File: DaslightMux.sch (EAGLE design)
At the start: 8 parts, among them U1 XC9572XL_TQ100

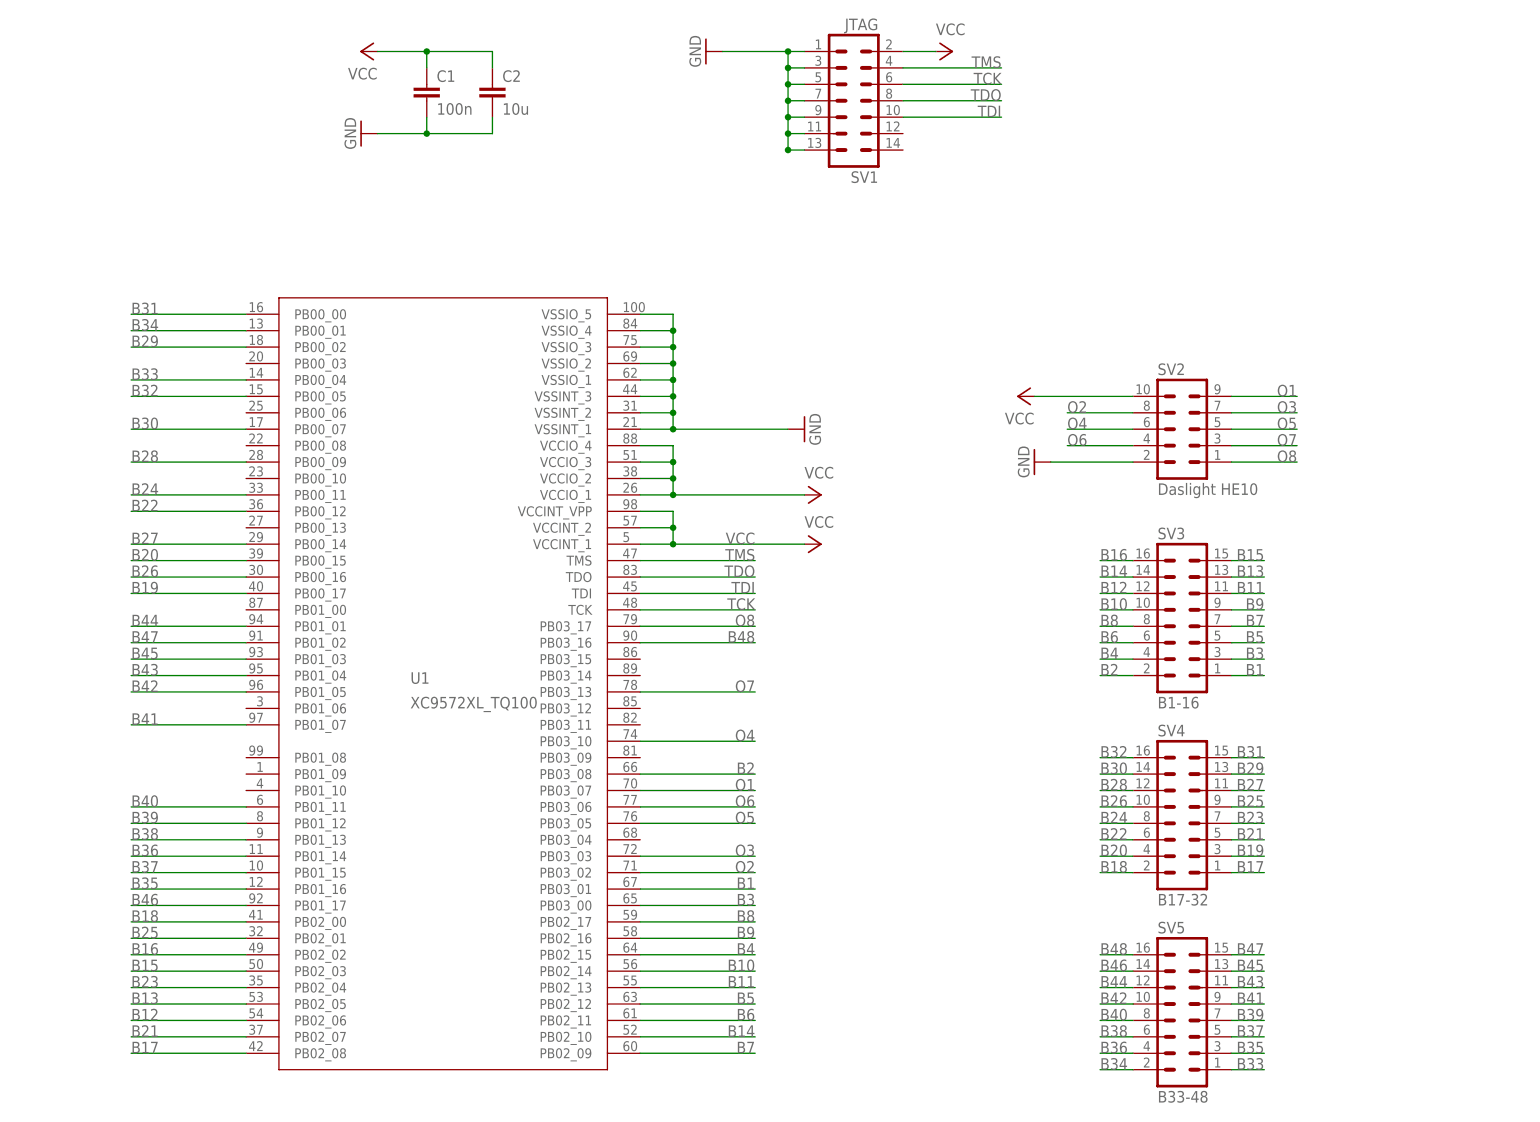
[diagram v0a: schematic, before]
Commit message: Cleanup, enclosure.
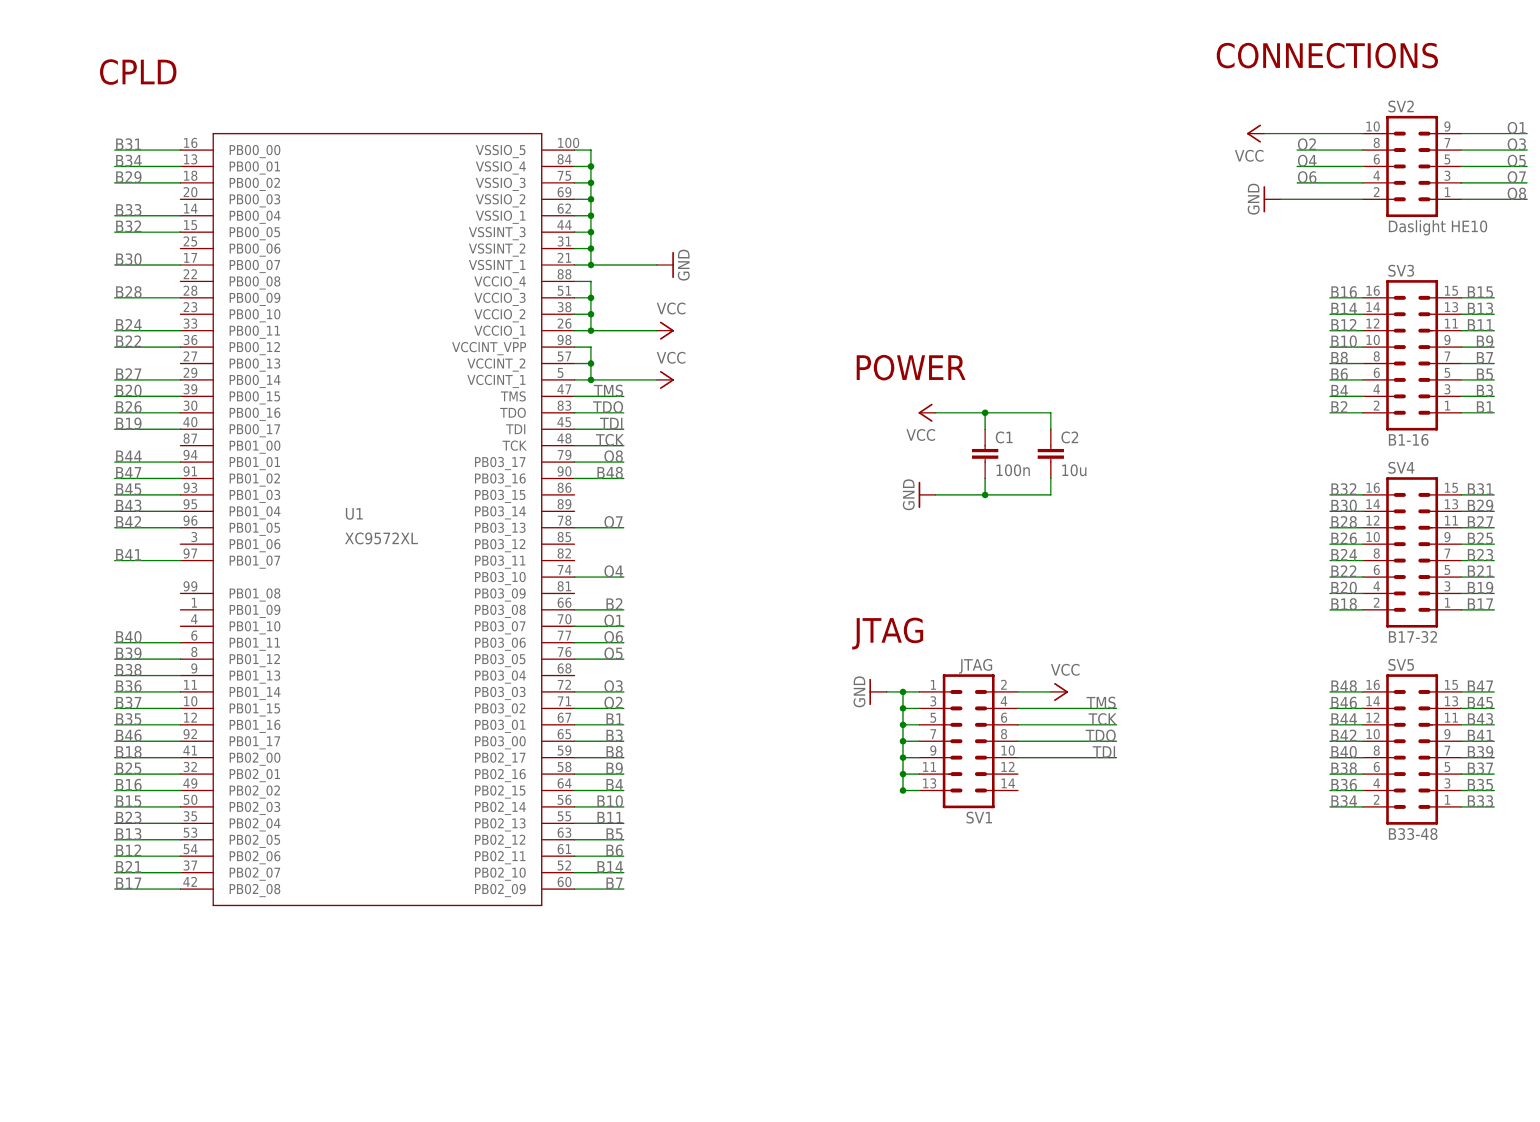
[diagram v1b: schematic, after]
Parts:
- U1: value XC9572XL_TQ100 -> XC9572XL
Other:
- note added: "CONNECTIONS"
- note added: "CPLD"
- note added: "JTAG"
- note added: "POWER"
- moved on the sheet: C1, C2, SV1, SV2, SV3, SV4, SV5, U1

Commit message: Schematic & enclosure
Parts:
- added EXT_VCC, GND: LSP10, solpad:LSP10
- added SJ1: (no value), jumper:SJ2W
- SV2: value Daslight HE10 -> HE10
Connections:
- new net N$1: SJ1.1, SV2.10
- new net N$2: EXT_VCC.MP, SJ1.3
- net GND: now also GND.MP
- net VCC: now also SJ1.2; no longer SV2.10
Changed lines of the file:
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@@
 <part name="GND2" library="supply1" deviceset="GND" device=""/>
 <part name="P+3" library="supply1" deviceset="VCC" device=""/>
-<part name="SV2" library="con-harting-ml" deviceset="ML10" device="" value="Daslight HE10"/>
+<part name="SV2" library="con-harting-ml" deviceset="ML10" device="" value="HE10"/>
 <part name="GND3" library="supply1" deviceset="GND" device=""/>
-<part name="P+4" library="supply1" deviceset="VCC" device=""/>
 <part name="SV3" library="con-harting-ml" deviceset="ML16" device="" value="B1-16"/>
 <part name="SV4" library="con-harting-ml" deviceset="ML16" device="" value="B17-32"/>
@@
 <part name="P+5" library="supply1" deviceset="VCC" device=""/>
 <part name="FRAME1" library="frames" deviceset="A4L-LOC" device="" value="Daslight MUX"/>
+<part name="SJ1" library="jumper" deviceset="SJ2W" device=""/>
+<part name="P+6" library="supply1" deviceset="VCC" device=""/>
+<part name="EXT_VCC" library="solpad" deviceset="LSP10" device=""/>
+<part name="GND" library="solpad" deviceset="LSP10" device=""/>
+<part name="GND5" library="supply1" deviceset="GND" device=""/>
 </parts>
 <sheets>
@@
 <instance part="SV2" gate="G$1" x="226.06" y="142.24"/>
 <instance part="GND3" gate="1" x="203.2" y="137.16" rot="R270"/>
-<instance part="P+4" gate="VCC" x="200.66" y="147.32" rot="R90"/>
 <instance part="SV3" gate="1" x="226.06" y="114.3"/>
 <instance part="SV4" gate="1" x="226.06" y="83.82"/>
@@
 <instance part="P+5" gate="VCC" x="149.86" y="104.14" rot="R90"/>
 <instance part="FRAME1" gate="G$1" x="0" y="0"/>
+<instance part="SJ1" gate="G$1" x="187.96" y="147.32" rot="R270"/>
+<instance part="P+6" gate="VCC" x="187.96" y="157.48"/>
+<instance part="EXT_VCC" gate="1" x="170.18" y="147.32" rot="R90"/>
+<instance part="GND" gate="1" x="170.18" y="142.24" rot="R90"/>
+<instance part="GND5" gate="1" x="175.26" y="142.24" rot="R90"/>
 </instances>
 <busses>
@@
 <junction x="160.02" y="91.44"/>
 </segment>
+<segment>
+<pinref part="GND" gate="1" pin="MP"/>
+<pinref part="GND5" gate="1" pin="GND"/>
+</segment>
 </net>
 <net name="TMS" class="0">
@@
 </segment>
 <segment>
-<pinref part="SV2" gate="G$1" pin="10"/>
-<pinref part="P+4" gate="VCC" pin="VCC"/>
-<wire x1="203.2" y1="147.32" x2="218.44" y2="147.32" width="0.1524" layer="91"/>
-</segment>
-<segment>
 <pinref part="P+5" gate="VCC" pin="VCC"/>
 <pinref part="C1" gate="G$1" pin="1"/>
@@
 <junction x="160.02" y="104.14"/>
 </segment>
+<segment>
+<pinref part="SJ1" gate="G$1" pin="2"/>
+<pinref part="P+6" gate="VCC" pin="VCC"/>
+<wire x1="187.96" y1="154.94" x2="187.96" y2="152.4" width="0.1524" layer="91"/>
+</segment>
 </net>
 <net name="B40" class="0">
@@
 </segment>
 </net>
+<net name="N$1" class="0">
+<segment>
+<pinref part="SV2" gate="G$1" pin="10"/>
+<wire x1="193.04" y1="147.32" x2="218.44" y2="147.32" width="0.1524" layer="91"/>
+<pinref part="SJ1" gate="G$1" pin="1"/>
+</segment>
+</net>
+<net name="N$2" class="0">
+<segment>
+<pinref part="SJ1" gate="G$1" pin="3"/>
+<wire x1="182.88" y1="147.32" x2="172.72" y2="147.32" width="0.1524" layer="91"/>
+<pinref part="EXT_VCC" gate="1" pin="MP"/>
+</segment>
+</net>

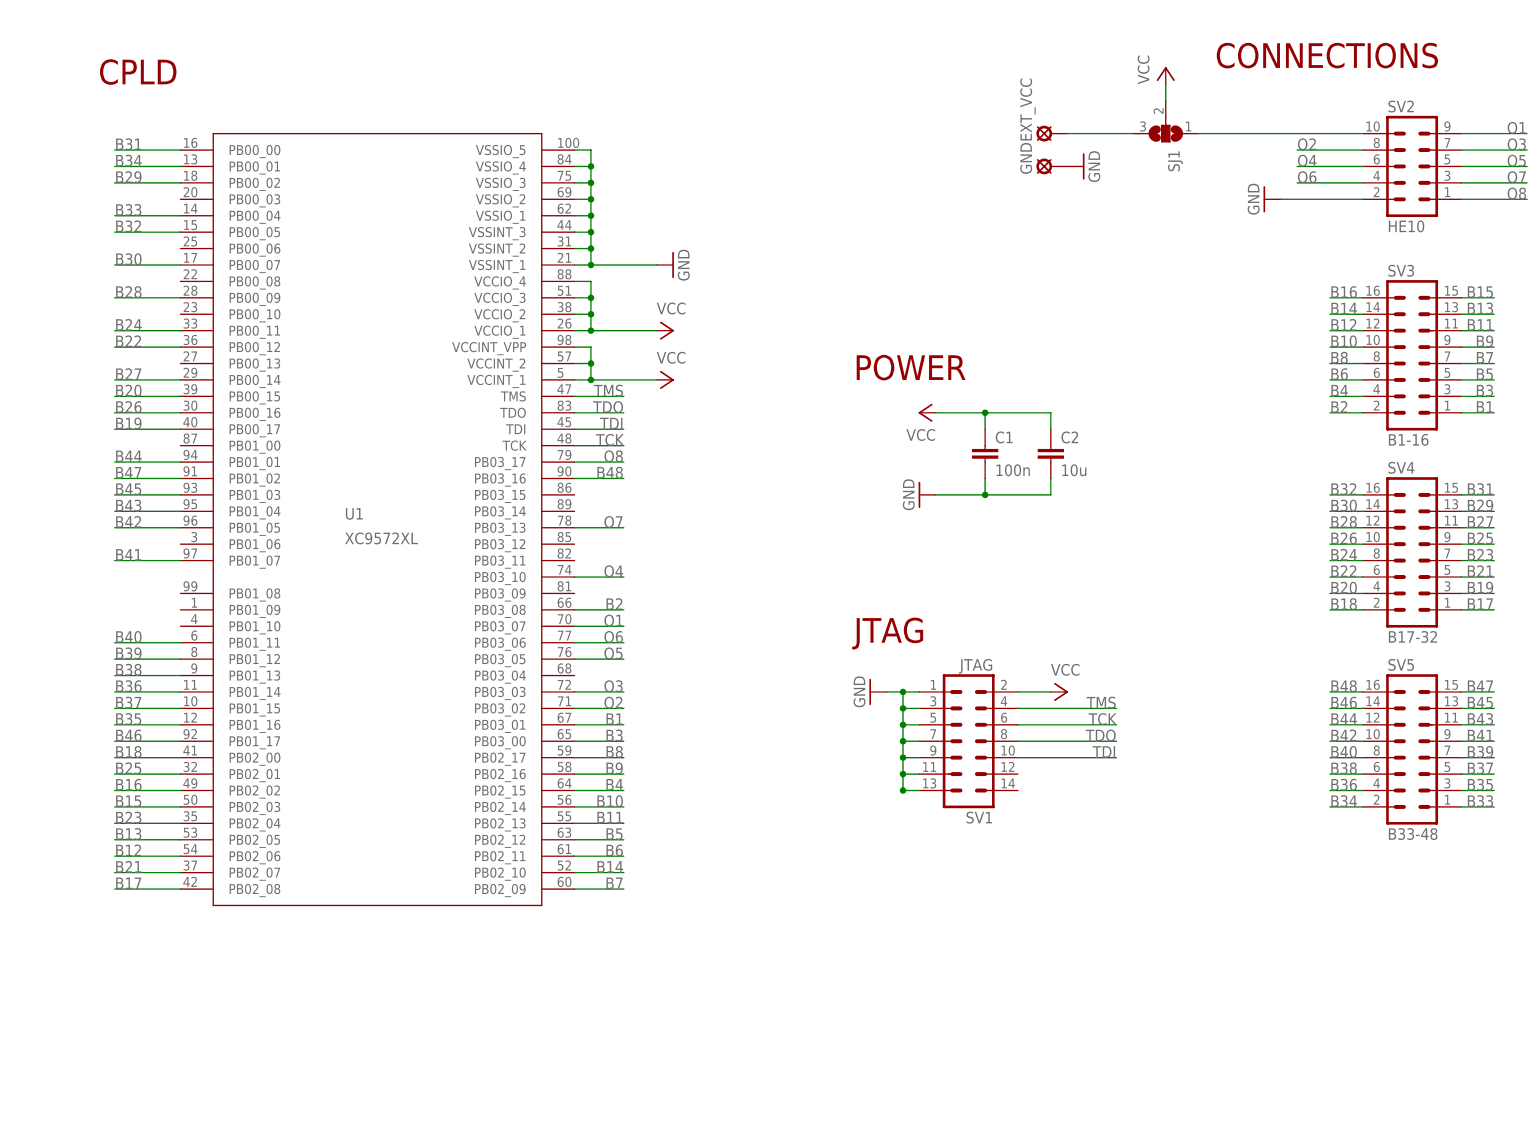
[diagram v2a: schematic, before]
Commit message: Changed to SUB-D, therefore swapped "all" pins
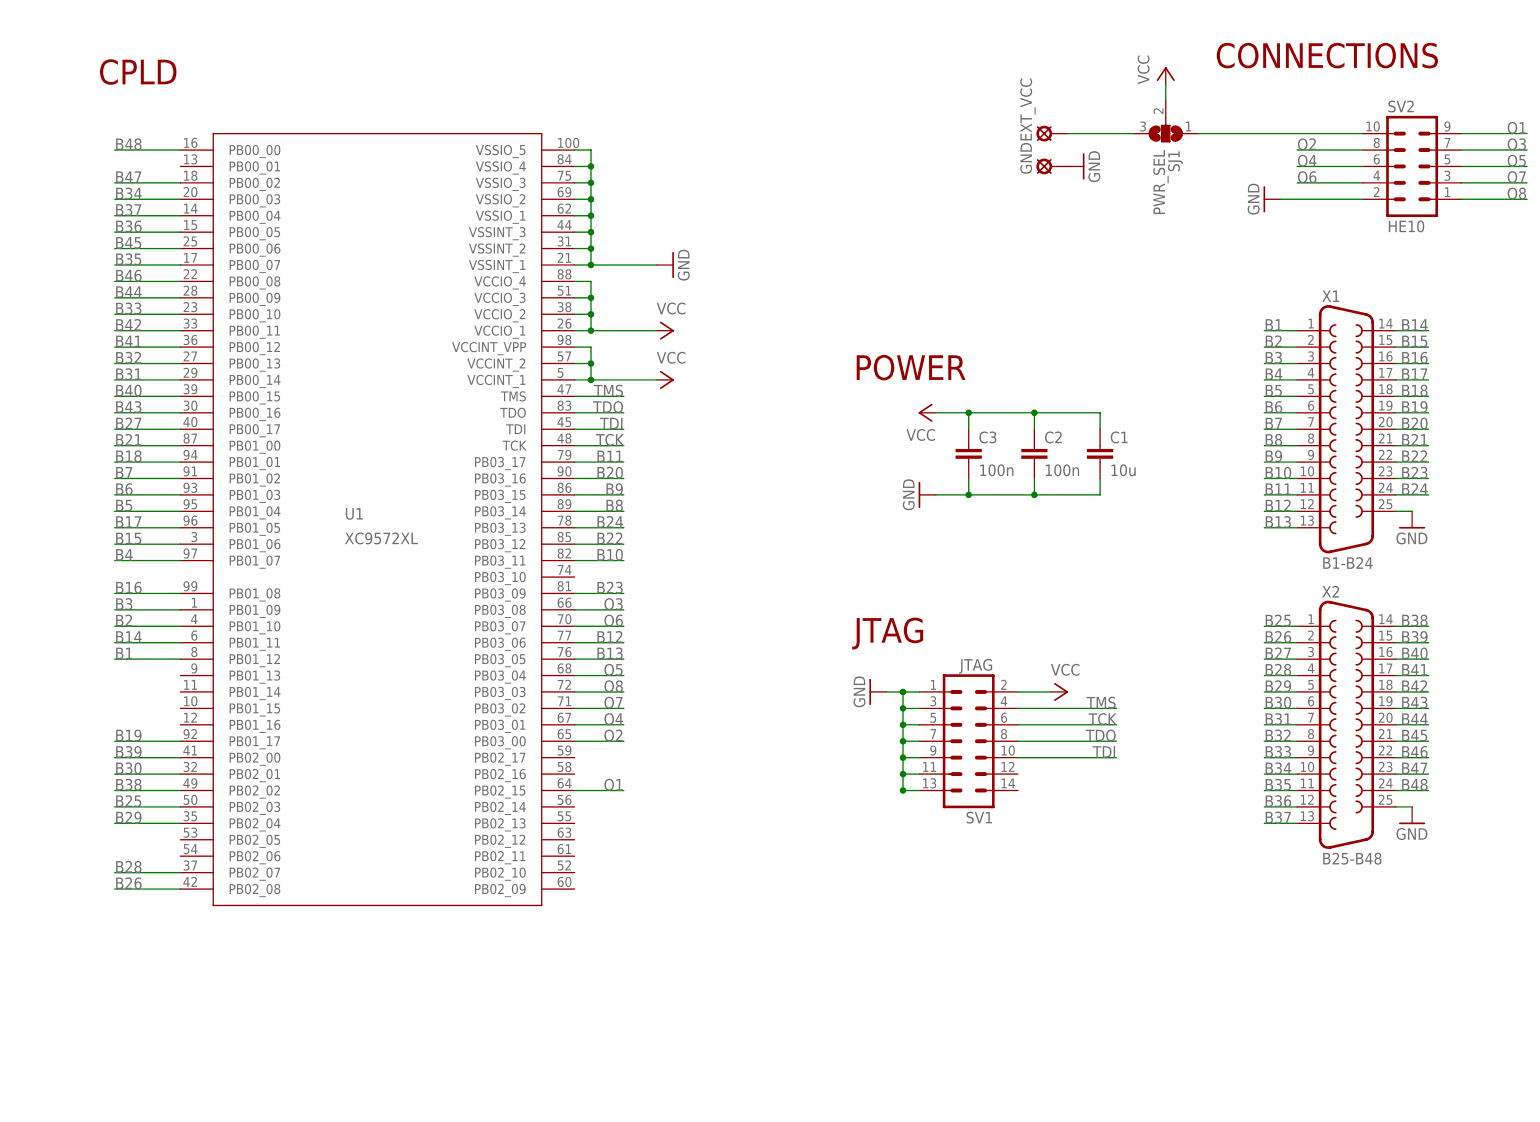
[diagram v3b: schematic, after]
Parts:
- removed SV3: B1-16, con-harting-ml:ML16
- removed SV4: B17-32, con-harting-ml:ML16
- removed SV5: B33-48, con-harting-ml:ML16
- added C3: 100n, resistor:C-EUC0603
- added X1: B1-B24, con-subd:F25HP
- added X2: B25-B48, con-subd:F25HP
- C1: value 100n -> 10u; device resistor:C-EUC0603 -> resistor:C-EUC1206
- C2: value 10u -> 100n; device resistor:C-EUC1206 -> resistor:C-EUC0603
- SJ1: value (none) -> PWR_SEL
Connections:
- net B1: now also U1.PB01_12, X1.1; no longer SV3.1, U1.PB03_01
- net B10: now also U1.PB03_11, X1.10; no longer SV3.10, U1.PB02_14
- net B11: now also U1.PB03_17, X1.11; no longer SV3.11, U1.PB02_13
- net B12: now also U1.PB03_06, X1.12; no longer SV3.12, U1.PB02_06
- net B13: now also U1.PB03_05, X1.13; no longer SV3.13, U1.PB02_05
- net B14: now also U1.PB01_11, X1.14; no longer SV3.14, U1.PB02_10
- net B15: now also U1.PB01_06, X1.15; no longer SV3.15, U1.PB02_03
- net B16: now also U1.PB01_08, X1.16; no longer SV3.16, U1.PB02_02
- net B17: now also U1.PB01_05, X1.17; no longer SV4.1, U1.PB02_08
- net B18: now also U1.PB01_01, X1.18; no longer SV4.2, U1.PB02_00
- net B19: now also U1.PB01_17, X1.19; no longer SV4.3, U1.PB00_17
- net B2: now also U1.PB01_10, X1.2; no longer SV3.2, U1.PB03_08
- net B20: now also U1.PB03_16, X1.20; no longer SV4.4, U1.PB00_15
- net B21: now also U1.PB01_00, X1.21; no longer SV4.5, U1.PB02_07
- net B22: now also U1.PB03_12, X1.22; no longer SV4.6, U1.PB00_12
- net B23: now also U1.PB03_09, X1.23; no longer SV4.7, U1.PB02_04
- net B24: now also U1.PB03_13, X1.24; no longer SV4.8, U1.PB00_11
- net B25: now also U1.PB02_03, X2.1; no longer SV4.9, U1.PB02_01
- net B26: now also U1.PB02_08, X2.2; no longer SV4.10, U1.PB00_16
- net B27: now also U1.PB00_17, X2.3; no longer SV4.11, U1.PB00_14
- net B28: now also U1.PB02_07, X2.4; no longer SV4.12, U1.PB00_09
- net B29: now also U1.PB02_04, X2.5; no longer SV4.13, U1.PB00_02
- net B3: now also U1.PB01_09, X1.3; no longer SV3.3, U1.PB03_00
- net B30: now also U1.PB02_01, X2.6; no longer SV4.14, U1.PB00_07
- net B31: now also U1.PB00_14, X2.7; no longer SV4.15, U1.PB00_00
- net B32: now also U1.PB00_13, X2.8; no longer SV4.16, U1.PB00_05
- net B33: now also U1.PB00_10, X2.9; no longer SV5.1, U1.PB00_04
- net B34: now also U1.PB00_03, X2.10; no longer SV5.2, U1.PB00_01
- net B35: now also U1.PB00_07, X2.11; no longer SV5.3, U1.PB01_16
- net B36: now also U1.PB00_05, X2.12; no longer SV5.4, U1.PB01_14
- net B37: now also U1.PB00_04, X2.13; no longer SV5.5, U1.PB01_15
- net B38: now also U1.PB02_02, X2.14; no longer SV5.6, U1.PB01_13
- net B39: now also U1.PB02_00, X2.15; no longer SV5.7, U1.PB01_12
- net B4: now also U1.PB01_07, X1.4; no longer SV3.4, U1.PB02_15
- net B40: now also U1.PB00_15, X2.16; no longer SV5.8, U1.PB01_11
- net B41: now also U1.PB00_12, X2.17; no longer SV5.9, U1.PB01_07
- net B42: now also U1.PB00_11, X2.18; no longer SV5.10, U1.PB01_05
- net B43: now also U1.PB00_16, X2.19; no longer SV5.11, U1.PB01_04
- net B44: now also U1.PB00_09, X2.20; no longer SV5.12, U1.PB01_01
- net B45: now also U1.PB00_06, X2.21; no longer SV5.13, U1.PB01_03
- net B46: now also U1.PB00_08, X2.22; no longer SV5.14, U1.PB01_17
- net B47: now also U1.PB00_02, X2.23; no longer SV5.15, U1.PB01_02
- net B48: now also U1.PB00_00, X2.24; no longer SV5.16, U1.PB03_16
- net B5: now also U1.PB01_04, X1.5; no longer SV3.5, U1.PB02_12
- net B6: now also U1.PB01_03, X1.6; no longer SV3.6, U1.PB02_11
- net B7: now also U1.PB01_02, X1.7; no longer SV3.7, U1.PB02_09
- net B8: now also U1.PB03_14, X1.8; no longer SV3.8, U1.PB02_17
- net B9: now also U1.PB03_15, X1.9; no longer SV3.9, U1.PB02_16
- net GND: now also C3.2, X1.25, X2.25
- net O1: now also U1.PB02_15; no longer U1.PB03_07
- net O2: now also U1.PB03_00; no longer U1.PB03_02
- net O3: now also U1.PB03_08; no longer U1.PB03_03
- net O4: now also U1.PB03_01; no longer U1.PB03_10
- net O5: now also U1.PB03_04; no longer U1.PB03_05
- net O6: now also U1.PB03_07; no longer U1.PB03_06
- net O7: now also U1.PB03_02; no longer U1.PB03_13
- net O8: now also U1.PB03_03; no longer U1.PB03_17
- net VCC: now also C3.1
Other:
- moved on the sheet: C1, C2
